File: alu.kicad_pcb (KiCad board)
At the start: 2 copper layers, 160 x 100 mm, 126 parts, among them U1 C96ABC, U10 74LS32, U11 74LS86, U12 74LS86, U13 74LS283, U14 74LS283, U15 74LS253, U16 74LS253, U17 74LS253, U18 74LS253, U2 74ACT04, U3 74ACT04, U4 74ACT158, U5 74ACT158, U6 74ACT158, U7 74LS08, U8 74LS08, U9 74LS32

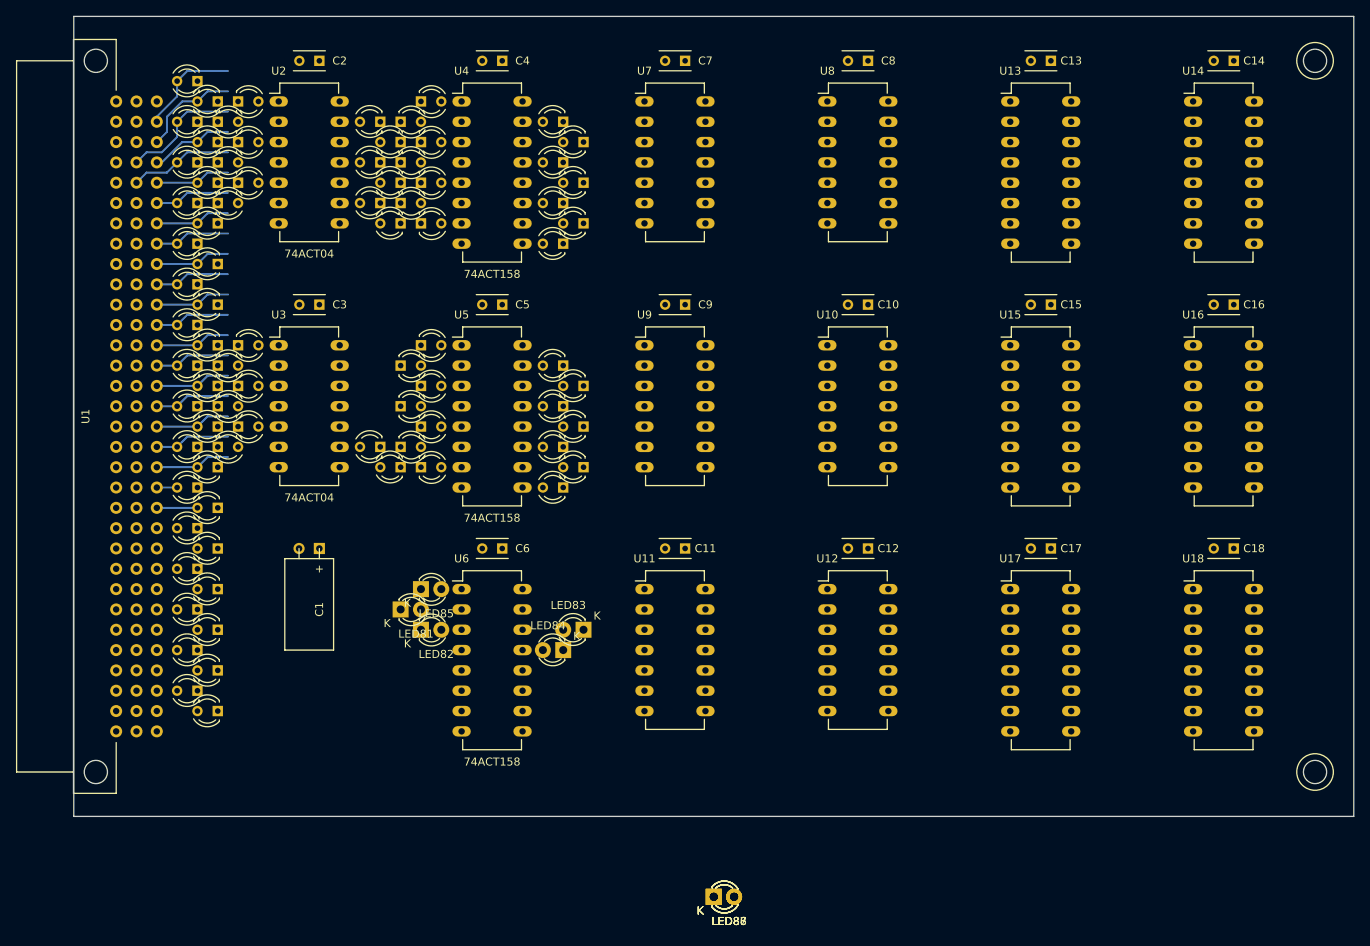
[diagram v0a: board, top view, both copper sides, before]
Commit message: component placement
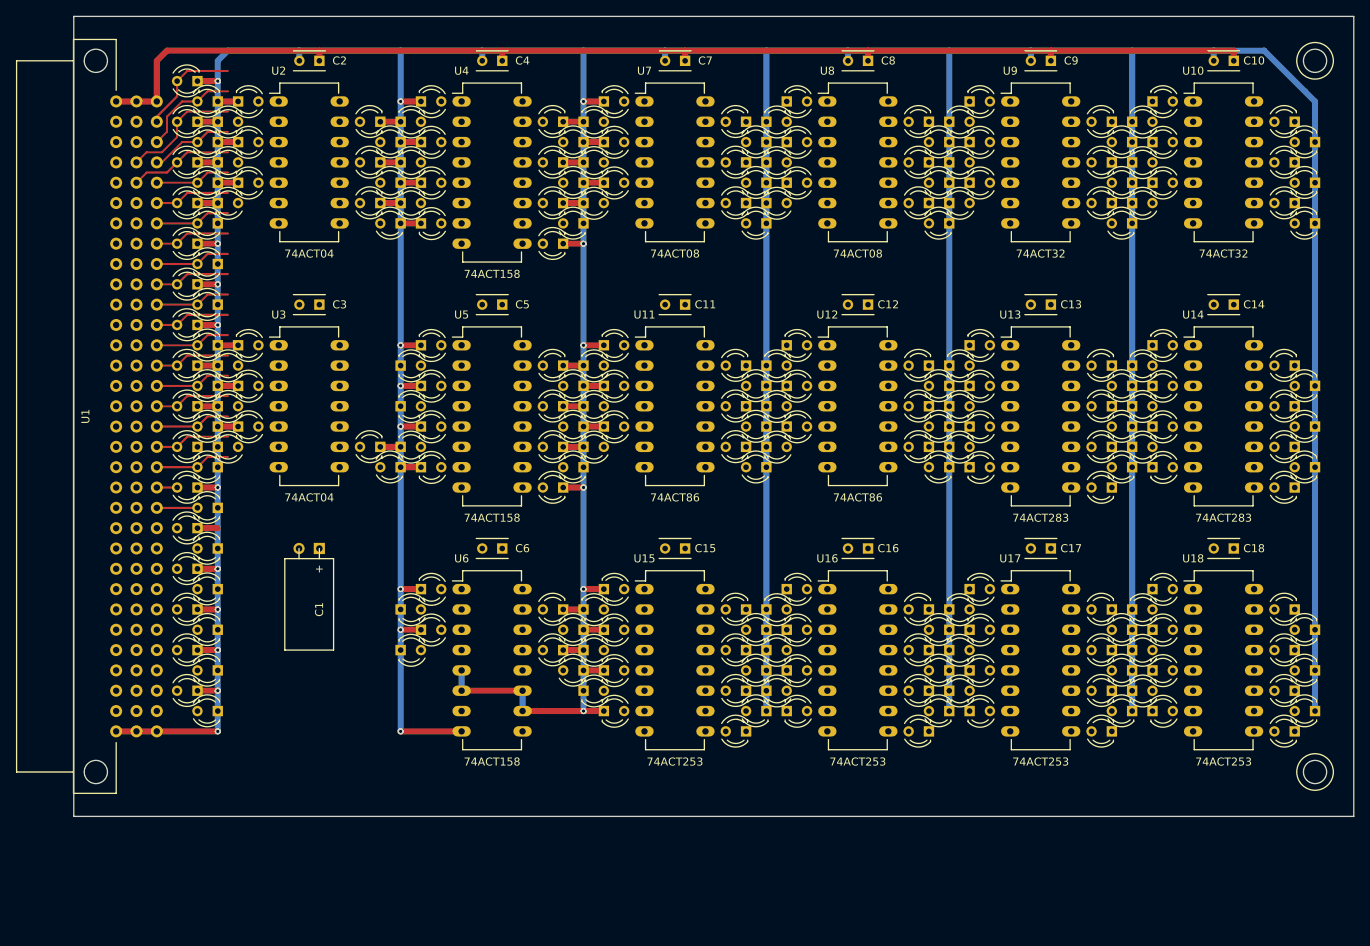
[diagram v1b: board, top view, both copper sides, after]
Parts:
- added LED100: DEBUG_LED, LEDs:LED-3MM, F.Cu at (159.1, 70.8)
- added LED101: DEBUG_LED, LEDs:LED-3MM, F.Cu at (176.9, 73.3)
- added LED102: DEBUG_LED, LEDs:LED-3MM, F.Cu at (179.4, 70.8)
- added LED103: DEBUG_LED, LEDs:LED-3MM, F.Cu at (179.4, 65.7)
- added LED104: DEBUG_LED, LEDs:LED-3MM, F.Cu at (176.9, 63.2)
- added LED105: DEBUG_LED, LEDs:LED-3MM, F.Cu at (136.3, 65.7)
- added LED106: DEBUG_LED, LEDs:LED-3MM, F.Cu at (133.7, 73.3)
- added LED107: DEBUG_LED, LEDs:LED-3MM, F.Cu at (156.6, 75.9)
- added LED108: DEBUG_LED, LEDs:LED-3MM, F.Cu at (154.0, 68.2)
- added LED109: DEBUG_LED, LEDs:LED-3MM, F.Cu at (159.1, 65.7)
- added LED110: DEBUG_LED, LEDs:LED-3MM, F.Cu at (156.6, 73.3)
- added LED111: DEBUG_LED, LEDs:LED-3MM, F.Cu at (179.4, 75.9)
- added LED112: DEBUG_LED, LEDs:LED-3MM, F.Cu at (176.9, 68.2)
- added LED113: DEBUG_LED, LEDs:LED-3MM, F.Cu at (182.0, 60.6)
- added LED114: DEBUG_LED, LEDs:LED-3MM, F.Cu at (179.4, 63.2)
- added LED115: DEBUG_LED, LEDs:LED-3MM, F.Cu at (179.4, 68.2)
- added LED116: DEBUG_LED, LEDs:LED-3MM, F.Cu at (182.0, 70.8)
- added LED117: DEBUG_LED, LEDs:LED-3MM, F.Cu at (199.8, 73.3)
- added LED118: DEBUG_LED, LEDs:LED-3MM, F.Cu at (202.3, 70.8)
- added LED119: DEBUG_LED, LEDs:LED-3MM, F.Cu at (202.3, 65.7)
- added LED120: DEBUG_LED, LEDs:LED-3MM, F.Cu at (199.8, 63.2)
- added LED121: DEBUG_LED, LEDs:LED-3MM, F.Cu at (204.8, 60.6)
- added LED122: DEBUG_LED, LEDs:LED-3MM, F.Cu at (202.3, 63.2)
- added LED123: DEBUG_LED, LEDs:LED-3MM, F.Cu at (202.3, 68.2)
- added LED124: DEBUG_LED, LEDs:LED-3MM, F.Cu at (204.8, 70.8)
- added LED125: DEBUG_LED, LEDs:LED-3MM, F.Cu at (222.6, 73.3)
- added LED126: DEBUG_LED, LEDs:LED-3MM, F.Cu at (225.2, 70.8)
- added LED127: DEBUG_LED, LEDs:LED-3MM, F.Cu at (225.2, 65.7)
- added LED128: DEBUG_LED, LEDs:LED-3MM, F.Cu at (222.6, 63.2)
- added LED129: DEBUG_LED, LEDs:LED-3MM, F.Cu at (182.0, 65.7)
- added LED130: DEBUG_LED, LEDs:LED-3MM, F.Cu at (179.4, 73.3)
- added LED131: DEBUG_LED, LEDs:LED-3MM, F.Cu at (202.3, 75.9)
- added LED132: DEBUG_LED, LEDs:LED-3MM, F.Cu at (199.8, 68.2)
- added LED133: DEBUG_LED, LEDs:LED-3MM, F.Cu at (204.8, 65.7)
- added LED134: DEBUG_LED, LEDs:LED-3MM, F.Cu at (202.3, 73.3)
- added LED135: DEBUG_LED, LEDs:LED-3MM, F.Cu at (225.2, 75.9)
- added LED136: DEBUG_LED, LEDs:LED-3MM, F.Cu at (222.6, 68.2)
- added LED137: DEBUG_LED, LEDs:LED-3MM, F.Cu at (136.3, 91.1)
- added LED138: DEBUG_LED, LEDs:LED-3MM, F.Cu at (133.7, 93.7)
- added LED139: DEBUG_LED, LEDs:LED-3MM, F.Cu at (133.7, 98.7)
- added LED140: DEBUG_LED, LEDs:LED-3MM, F.Cu at (136.3, 101.3)
- added LED141: DEBUG_LED, LEDs:LED-3MM, F.Cu at (154.0, 103.8)
- added LED142: DEBUG_LED, LEDs:LED-3MM, F.Cu at (156.6, 101.3)
- added LED143: DEBUG_LED, LEDs:LED-3MM, F.Cu at (156.6, 96.2)
- added LED144: DEBUG_LED, LEDs:LED-3MM, F.Cu at (154.0, 93.7)
- added LED145: DEBUG_LED, LEDs:LED-3MM, F.Cu at (159.1, 91.1)
- added LED146: DEBUG_LED, LEDs:LED-3MM, F.Cu at (156.6, 93.7)
- added LED147: DEBUG_LED, LEDs:LED-3MM, F.Cu at (156.6, 98.7)
- added LED148: DEBUG_LED, LEDs:LED-3MM, F.Cu at (159.1, 101.3)
- added LED149: DEBUG_LED, LEDs:LED-3MM, F.Cu at (176.9, 103.8)
- added LED150: DEBUG_LED, LEDs:LED-3MM, F.Cu at (179.4, 101.3)
- added LED151: DEBUG_LED, LEDs:LED-3MM, F.Cu at (179.4, 96.2)
- added LED152: DEBUG_LED, LEDs:LED-3MM, F.Cu at (176.9, 93.7)
- added LED153: DEBUG_LED, LEDs:LED-3MM, F.Cu at (136.3, 96.2)
- added LED154: DEBUG_LED, LEDs:LED-3MM, F.Cu at (133.7, 103.8)
- added LED155: DEBUG_LED, LEDs:LED-3MM, F.Cu at (156.6, 106.3)
- added LED156: DEBUG_LED, LEDs:LED-3MM, F.Cu at (154.0, 98.7)
- added LED157: DEBUG_LED, LEDs:LED-3MM, F.Cu at (159.1, 96.2)
- added LED158: DEBUG_LED, LEDs:LED-3MM, F.Cu at (156.6, 103.8)
- added LED159: DEBUG_LED, LEDs:LED-3MM, F.Cu at (179.4, 106.3)
- added LED160: DEBUG_LED, LEDs:LED-3MM, F.Cu at (176.9, 98.7)
- added LED161: DEBUG_LED, LEDs:LED-3MM, F.Cu at (182.0, 106.3)
- added LED162: DEBUG_LED, LEDs:LED-3MM, F.Cu at (182.0, 101.3)
- added LED163: DEBUG_LED, LEDs:LED-3MM, F.Cu at (182.0, 96.2)
- added LED164: DEBUG_LED, LEDs:LED-3MM, F.Cu at (202.3, 96.2)
- added LED165: DEBUG_LED, LEDs:LED-3MM, F.Cu at (202.3, 101.3)
- added LED166: DEBUG_LED, LEDs:LED-3MM, F.Cu at (179.4, 103.8)
- added LED167: DEBUG_LED, LEDs:LED-3MM, F.Cu at (179.4, 93.7)
- added LED168: DEBUG_LED, LEDs:LED-3MM, F.Cu at (199.8, 93.7)
- added LED169: DEBUG_LED, LEDs:LED-3MM, F.Cu at (199.8, 103.8)
- added LED170: DEBUG_LED, LEDs:LED-3MM, F.Cu at (204.8, 106.3)
- added LED171: DEBUG_LED, LEDs:LED-3MM, F.Cu at (204.8, 101.3)
- added LED172: DEBUG_LED, LEDs:LED-3MM, F.Cu at (204.8, 96.2)
- added LED173: DEBUG_LED, LEDs:LED-3MM, F.Cu at (225.2, 96.2)
- added LED174: DEBUG_LED, LEDs:LED-3MM, F.Cu at (225.2, 101.3)
- added LED175: DEBUG_LED, LEDs:LED-3MM, F.Cu at (202.3, 103.8)
- added LED176: DEBUG_LED, LEDs:LED-3MM, F.Cu at (202.3, 93.7)
- added LED177: DEBUG_LED, LEDs:LED-3MM, F.Cu at (222.6, 93.7)
- added LED178: DEBUG_LED, LEDs:LED-3MM, F.Cu at (222.6, 103.8)
- added LED179: DEBUG_LED, LEDs:LED-3MM, F.Cu at (179.4, 98.7)
- added LED180: DEBUG_LED, LEDs:LED-3MM, F.Cu at (182.0, 91.1)
- added LED181: DEBUG_LED, LEDs:LED-3MM, F.Cu at (199.8, 98.7)
- added LED182: DEBUG_LED, LEDs:LED-3MM, F.Cu at (202.3, 106.3)
- added LED183: DEBUG_LED, LEDs:LED-3MM, F.Cu at (199.8, 108.9)
- added LED184: DEBUG_LED, LEDs:LED-3MM, F.Cu at (202.3, 98.7)
- added LED185: DEBUG_LED, LEDs:LED-3MM, F.Cu at (204.8, 91.1)
- added LED186: DEBUG_LED, LEDs:LED-3MM, F.Cu at (222.6, 98.7)
- added LED187: DEBUG_LED, LEDs:LED-3MM, F.Cu at (225.2, 106.3)
- added LED188: DEBUG_LED, LEDs:LED-3MM, F.Cu at (222.6, 108.9)
- added LED189: DEBUG_LED, LEDs:LED-3MM, F.Cu at (133.7, 134.3)
- added LED190: DEBUG_LED, LEDs:LED-3MM, F.Cu at (136.3, 131.8)
- added LED191: DEBUG_LED, LEDs:LED-3MM, F.Cu at (133.7, 129.2)
- added LED192: DEBUG_LED, LEDs:LED-3MM, F.Cu at (136.3, 126.7)
- added LED193: DEBUG_LED, LEDs:LED-3MM, F.Cu at (136.3, 121.6)
- added LED194: DEBUG_LED, LEDs:LED-3MM, F.Cu at (156.6, 136.8)
- added LED195: DEBUG_LED, LEDs:LED-3MM, F.Cu at (154.0, 134.3)
- added LED196: DEBUG_LED, LEDs:LED-3MM, F.Cu at (156.6, 131.8)
- added LED197: DEBUG_LED, LEDs:LED-3MM, F.Cu at (154.0, 129.2)
- added LED198: DEBUG_LED, LEDs:LED-3MM, F.Cu at (154.0, 124.1)
- added LED199: DEBUG_LED, LEDs:LED-3MM, F.Cu at (156.6, 126.7)
- added LED200: DEBUG_LED, LEDs:LED-3MM, F.Cu at (133.7, 124.1)
- added LED201: DEBUG_LED, LEDs:LED-3MM, F.Cu at (156.6, 134.3)
- added LED202: DEBUG_LED, LEDs:LED-3MM, F.Cu at (159.1, 131.8)
- added LED203: DEBUG_LED, LEDs:LED-3MM, F.Cu at (156.6, 129.2)
- added LED204: DEBUG_LED, LEDs:LED-3MM, F.Cu at (159.1, 126.7)
- added LED205: DEBUG_LED, LEDs:LED-3MM, F.Cu at (159.1, 121.6)
- added LED206: DEBUG_LED, LEDs:LED-3MM, F.Cu at (179.4, 136.8)
- added LED207: DEBUG_LED, LEDs:LED-3MM, F.Cu at (176.9, 134.3)
- added LED208: DEBUG_LED, LEDs:LED-3MM, F.Cu at (179.4, 131.8)
- added LED209: DEBUG_LED, LEDs:LED-3MM, F.Cu at (176.9, 129.2)
- added LED210: DEBUG_LED, LEDs:LED-3MM, F.Cu at (176.9, 124.1)
- added LED211: DEBUG_LED, LEDs:LED-3MM, F.Cu at (179.4, 126.7)
- added LED212: DEBUG_LED, LEDs:LED-3MM, F.Cu at (156.6, 124.1)
- added LED213: DEBUG_LED, LEDs:LED-3MM, F.Cu at (179.4, 134.3)
- added LED214: DEBUG_LED, LEDs:LED-3MM, F.Cu at (182.0, 131.8)
- added LED215: DEBUG_LED, LEDs:LED-3MM, F.Cu at (179.4, 129.2)
- added LED216: DEBUG_LED, LEDs:LED-3MM, F.Cu at (182.0, 126.7)
- added LED217: DEBUG_LED, LEDs:LED-3MM, F.Cu at (182.0, 121.6)
- added LED218: DEBUG_LED, LEDs:LED-3MM, F.Cu at (202.3, 136.8)
- added LED219: DEBUG_LED, LEDs:LED-3MM, F.Cu at (199.8, 134.3)
- added LED220: DEBUG_LED, LEDs:LED-3MM, F.Cu at (202.3, 131.8)
- added LED221: DEBUG_LED, LEDs:LED-3MM, F.Cu at (199.8, 129.2)
- added LED222: DEBUG_LED, LEDs:LED-3MM, F.Cu at (199.8, 124.1)
- added LED223: DEBUG_LED, LEDs:LED-3MM, F.Cu at (202.3, 126.7)
- added LED224: DEBUG_LED, LEDs:LED-3MM, F.Cu at (179.4, 124.1)
- added LED225: DEBUG_LED, LEDs:LED-3MM, F.Cu at (202.3, 134.3)
- added LED226: DEBUG_LED, LEDs:LED-3MM, F.Cu at (204.8, 131.8)
- added LED227: DEBUG_LED, LEDs:LED-3MM, F.Cu at (202.3, 129.2)
- added LED228: DEBUG_LED, LEDs:LED-3MM, F.Cu at (204.8, 126.7)
- added LED229: DEBUG_LED, LEDs:LED-3MM, F.Cu at (204.8, 121.6)
- added LED230: DEBUG_LED, LEDs:LED-3MM, F.Cu at (225.2, 136.8)
- added LED231: DEBUG_LED, LEDs:LED-3MM, F.Cu at (222.6, 134.3)
- added LED232: DEBUG_LED, LEDs:LED-3MM, F.Cu at (225.2, 131.8)
- added LED233: DEBUG_LED, LEDs:LED-3MM, F.Cu at (222.6, 129.2)
- added LED234: DEBUG_LED, LEDs:LED-3MM, F.Cu at (222.6, 124.1)
- added LED235: DEBUG_LED, LEDs:LED-3MM, F.Cu at (225.2, 126.7)
- added LED236: DEBUG_LED, LEDs:LED-3MM, F.Cu at (202.3, 124.1)
- added LED237: DEBUG_LED, LEDs:LED-3MM, F.Cu at (136.3, 136.8)
- added LED238: DEBUG_LED, LEDs:LED-3MM, F.Cu at (154.0, 139.4)
- added LED239: DEBUG_LED, LEDs:LED-3MM, F.Cu at (159.1, 136.8)
- added LED240: DEBUG_LED, LEDs:LED-3MM, F.Cu at (176.9, 139.4)
- added LED241: DEBUG_LED, LEDs:LED-3MM, F.Cu at (182.0, 136.8)
- added LED242: DEBUG_LED, LEDs:LED-3MM, F.Cu at (199.8, 139.4)
- added LED243: DEBUG_LED, LEDs:LED-3MM, F.Cu at (204.8, 136.8)
- added LED244: DEBUG_LED, LEDs:LED-3MM, F.Cu at (222.6, 139.4)
- added LED89: DEBUG_LED, LEDs:LED-3MM, F.Cu at (136.3, 60.6)
- added LED90: DEBUG_LED, LEDs:LED-3MM, F.Cu at (133.7, 63.2)
- added LED91: DEBUG_LED, LEDs:LED-3MM, F.Cu at (133.7, 68.2)
- added LED92: DEBUG_LED, LEDs:LED-3MM, F.Cu at (136.3, 70.8)
- added LED93: DEBUG_LED, LEDs:LED-3MM, F.Cu at (154.0, 73.3)
- added LED94: DEBUG_LED, LEDs:LED-3MM, F.Cu at (156.6, 70.8)
- added LED95: DEBUG_LED, LEDs:LED-3MM, F.Cu at (156.6, 65.7)
- added LED96: DEBUG_LED, LEDs:LED-3MM, F.Cu at (154.0, 63.2)
- added LED97: DEBUG_LED, LEDs:LED-3MM, F.Cu at (159.1, 60.6)
- added LED98: DEBUG_LED, LEDs:LED-3MM, F.Cu at (156.6, 63.2)
- added LED99: DEBUG_LED, LEDs:LED-3MM, F.Cu at (156.6, 68.2)
- U10, U9: value 74LS32 -> 74ACT32
- U11, U12: value 74LS86 -> 74ACT86
- U13, U14: value 74LS283 -> 74ACT283
- U15, U16, U17, U18: value 74LS253 -> 74ACT253
- U7, U8: value 74LS08 -> 74ACT08
- moved C10 54.9 mm to (215.0, 55.5)
- moved C15 54.9 mm to (146.4, 116.5)
- moved C16 54.9 mm to (169.3, 116.5)
- moved C9 54.9 mm to (192.1, 55.5)
- moved U10 54.9 mm to (209.9, 60.6)
- moved U15 54.9 mm to (141.3, 121.6)
- moved U16 54.9 mm to (164.2, 121.6)
- moved U9 54.9 mm to (187.1, 60.6)
- moved LED87 49.8 mm to (110.9, 129.2)
- moved LED86 40.6 mm to (131.2, 124.1), turned to 180 degrees
- moved LED88 32.6 mm to (133.7, 131.8), turned to 180 degrees
- moved C11 30.5 mm to (146.4, 86.0)
- moved C12 30.5 mm to (169.3, 86.0)
- moved C13 30.5 mm to (192.1, 86.0)
- moved C14 30.5 mm to (215.0, 86.0)
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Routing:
- net GND: track 0.00 -> 903.8 mm, vias 0 -> 24
- net VCC: track 0.00 -> 152.9 mm
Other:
- net class Power added: clearance 0.175, trace_width 0.75, via_dia 0.8, via_drill 0.4

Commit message: pcb routing
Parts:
- moved LED31 3.59 mm to (88.0, 136.8)
- moved LED11 3.59 mm to (88.0, 86.0)
- moved LED13 3.59 mm to (88.0, 91.1)
- moved LED14 3.59 mm to (85.5, 93.7)
- moved LED16 3.59 mm to (85.5, 98.7)
- moved LED18 3.59 mm to (85.5, 103.8)
- moved LED20 3.59 mm to (85.5, 108.9)
- moved LED21 3.59 mm to (88.0, 111.4)
- moved LED23 3.59 mm to (88.0, 116.5)
- moved LED25 3.59 mm to (88.0, 121.6)
- moved LED27 3.59 mm to (88.0, 126.7)
- moved LED28 3.59 mm to (85.5, 129.2)
- moved LED3 3.59 mm to (85.5, 68.2)
- moved LED5 3.59 mm to (88.0, 70.8)
- moved LED7 3.59 mm to (88.0, 75.9)
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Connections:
- U1 pad A1: GND -> Net-(U1-PadA1)
- U1 pad A31: Net-(U1-PadA31) -> GND
- U1 pad B1: GND -> Net-(U1-PadB1)
- U1 pad B27: Net-(U1-PadB27) -> /BFF
- U1 pad B28: /BFF -> /CSET
- U1 pad B29: /CSET -> Net-(U1-PadB29)
- U1 pad B31: Net-(U1-PadB31) -> GND
- U1 pad C1: GND -> /COX
- U1 pad C10: /Z0 -> /CIX
- U1 pad C11: /CIX -> /BX7
- U1 pad C12: /BX7 -> /BX6
- U1 pad C13: /BX6 -> /BX5
- U1 pad C14: /BX5 -> /BX4
- U1 pad C15: /BX4 -> /BX3
- U1 pad C16: /BX3 -> /BX2
- U1 pad C17: /BX2 -> /BX1
- U1 pad C18: /BX1 -> /BX0
- U1 pad C19: /BX0 -> /A7
- U1 pad C2: /COX -> /Z7
- U1 pad C20: /A7 -> /A6
- U1 pad C21: /A6 -> /A5
- U1 pad C22: /A5 -> /A4
- U1 pad C23: /A4 -> /A3
- U1 pad C24: /A3 -> /A2
- U1 pad C25: /A2 -> /A1
- U1 pad C26: /A1 -> /A0
- U1 pad C27: /A0 -> /~INV
- U1 pad C28: /~INV -> /Y1
- U1 pad C29: /Y1 -> /Y0
- U1 pad C3: /Z7 -> /Z6
- U1 pad C30: /Y0 -> /~OE
- U1 pad C31: /~OE -> GND
- U1 pad C4: /Z6 -> /Z5
- U1 pad C5: /Z5 -> /Z4
- U1 pad C6: /Z4 -> /Z3
- U1 pad C7: /Z3 -> /Z2
- U1 pad C8: /Z2 -> /Z1
- U1 pad C9: /Z1 -> /Z0
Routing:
- net GND: track 903.8 -> 1373.9 mm, vias 24 -> 62
- net VCC: track 152.9 -> 587.3 mm, vias 0 -> 17
- net /B3: track 0.00 -> 149.7 mm, vias 0 -> 1
- net /A1: track 9.42 -> 102.7 mm
- net /A5: track 9.42 -> 102.7 mm, vias 0 -> 1
- net /B2: track 0.00 -> 93.3 mm
- net /B1: track 0.00 -> 90.6 mm
- net /A7: track 9.42 -> 97.9 mm
- net /B4: track 0.00 -> 88.5 mm
- net /~OE: track 13.0 -> 97.3 mm
- net /A0: track 9.42 -> 93.0 mm
- net /A3: track 9.42 -> 92.8 mm
- net /A6: track 9.42 -> 92.6 mm
- net /A2: track 9.42 -> 92.4 mm
- net /A4: track 9.42 -> 90.3 mm
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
